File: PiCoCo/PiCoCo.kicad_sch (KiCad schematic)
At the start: 63 parts, among them J1 EXP (Plus-W), P1 COCO-CART, Q2 2N7002, Q3 2N7002, Q4 2N7002, U1 Pico 2 / RP2350B-Plus-W, U10 SN74LVC245A, U11 SN74LVC245A, U12 SN74LVC245A, U13 SN74LVC245A, U14 AMS1117-3.3, U15 SN74LVC00A

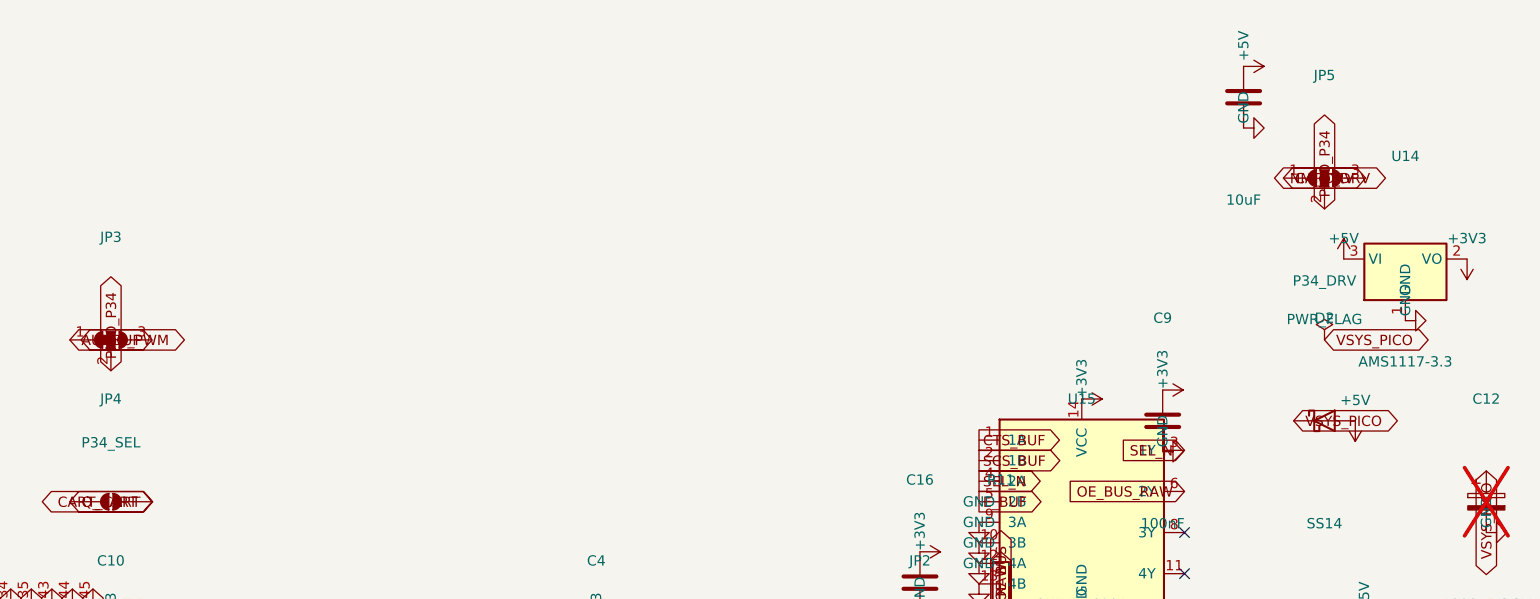
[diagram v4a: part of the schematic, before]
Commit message: v2.3.1: J2/J3 DNP 1x3 pin-header twins of JP3/JP5 (movable shunt option)
Same nets as the solder jumpers; fit at most one of each pair. Re-routed;
DRC 0 errors / 0 unconnected / 0 parity; GND coverage under the bus 40%
(was 27%). BOM/CPL unchanged (17 lines / 38 parts, headers are DNP).

Co-Authored-By: Claude Fable 5.1 <noreply@anthropic.com>
Claude-Session: https://claude.ai/code/session_013jbrP69zFzwzxjawTKy2c7
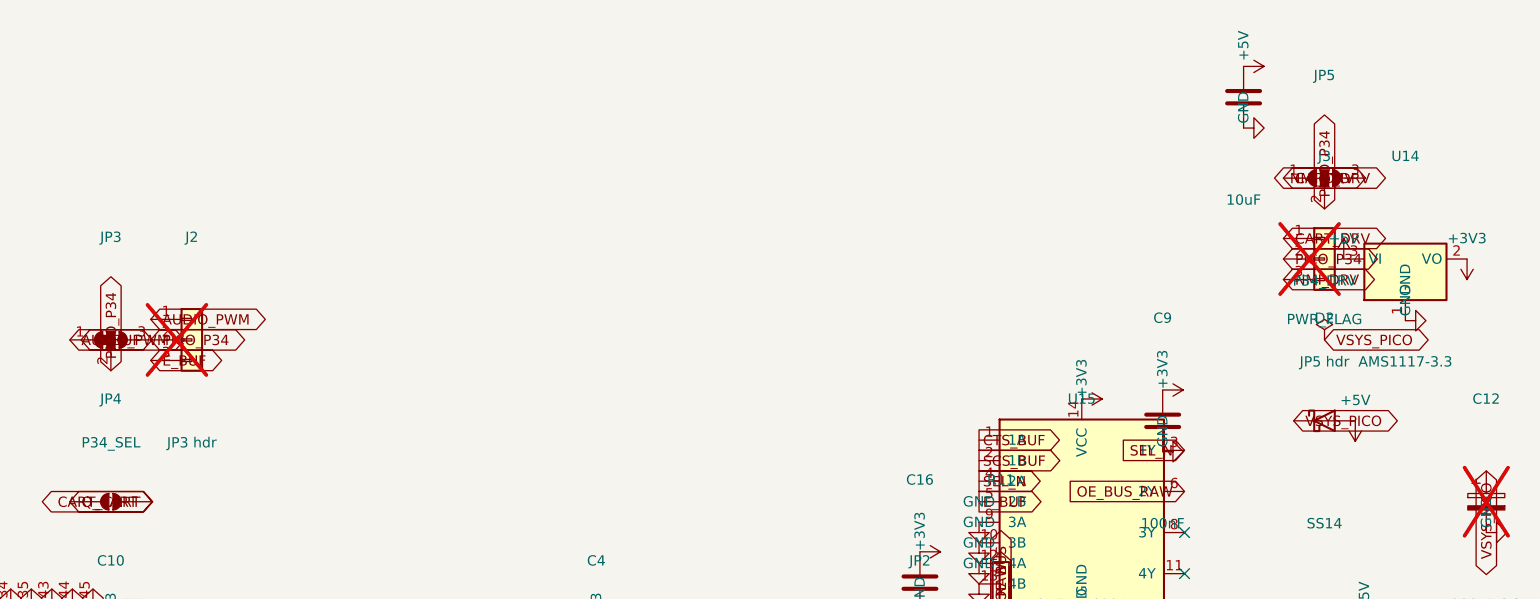
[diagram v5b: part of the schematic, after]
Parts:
- added J2: JP3 hdr, Connector_PinHeader_2.54mm:PinHeader_1x03_P2.54mm_Vertical, symbol Connector_Generic:Conn_01x03
- added J3: JP5 hdr, Connector_PinHeader_2.54mm:PinHeader_1x03_P2.54mm_Vertical, symbol Connector_Generic:Conn_01x03
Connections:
- net AUDIO_PWM: now also J2.1 (Pin_1)
- net CART_DRV: now also J3.1 (Pin_1)
- net E_BUF: now also J2.3 (Pin_3)
- net NMI_DRV: now also J3.3 (Pin_3)
- net PICO_P34: now also J2.2 (Pin_2), J3.2 (Pin_2)
